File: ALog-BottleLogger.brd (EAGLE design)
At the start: 120.7 x 44.5 mm, 102 parts, among them IC2 ATMEGA644M, Q1 220mA/50V/3.5Ω, Q11 220mA/50V/3.5Ω, Q12 4.3A/20V/54mΩ, Q5 4.3A/20V/54mΩ, Q6 4.3A/20V/54mΩ, Q7 4.3A/20V/54mΩ, Q8 220mA/50V/3.5Ω, Q9 220mA/50V/3.5Ω, U2 FT231X-Q

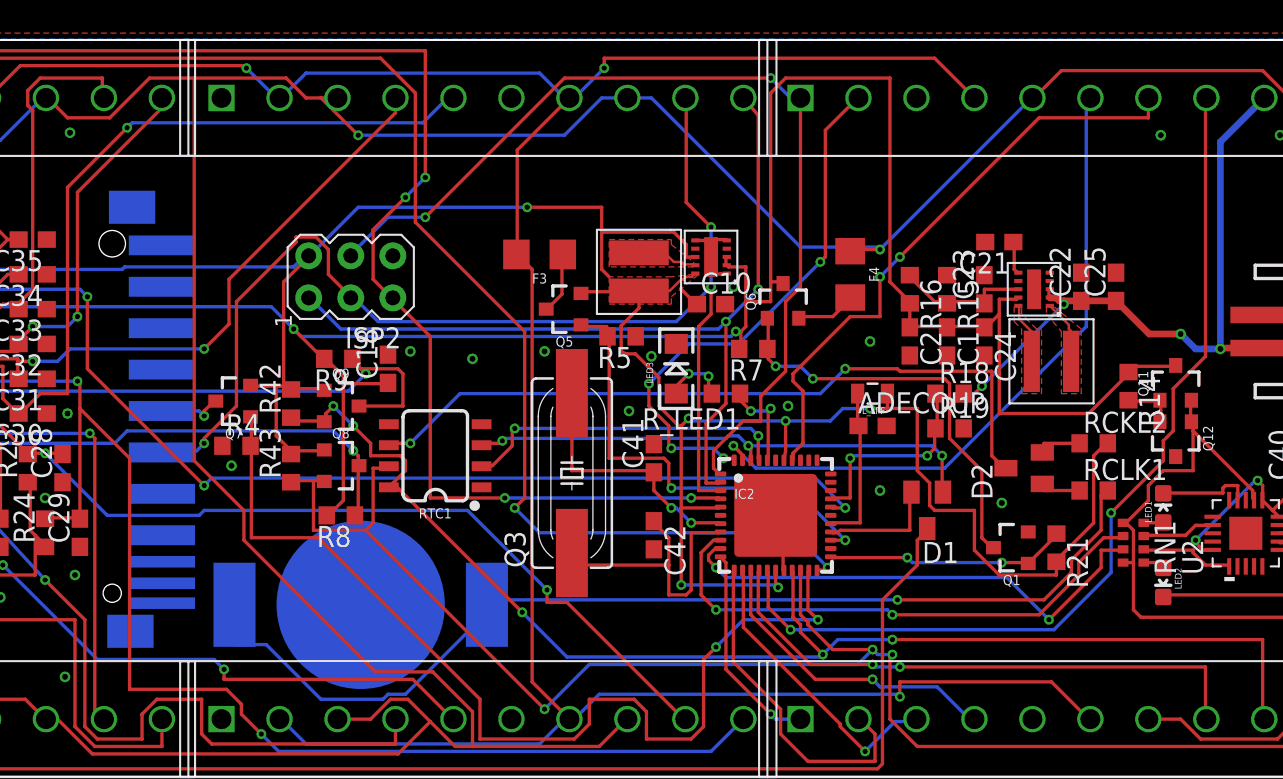
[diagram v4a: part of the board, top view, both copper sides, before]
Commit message: Changed cap sizes on 10 and 22 uF to 805 and fixed MISO/MOSI labels on SD card.
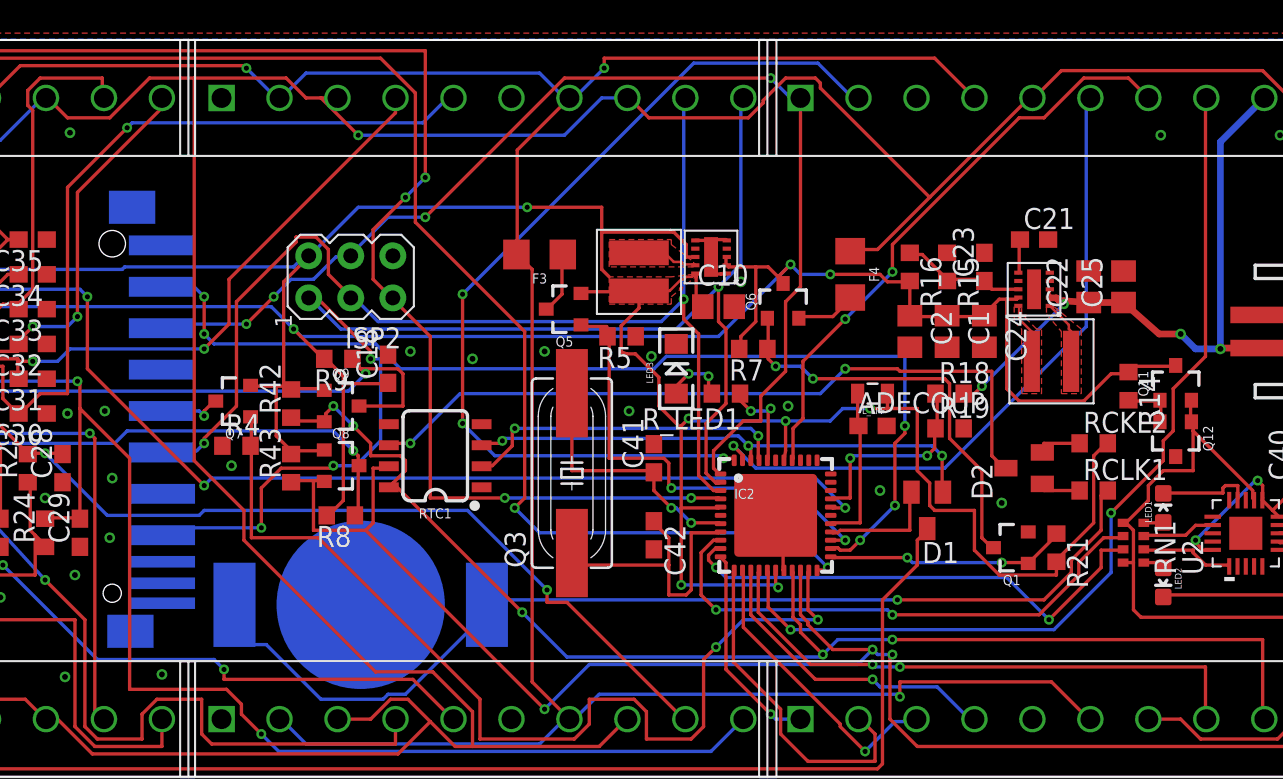
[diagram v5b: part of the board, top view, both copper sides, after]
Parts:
- C1, C10, C2, C22, C24, C25: device rcl:C0603 -> rcl:C0805
- C12, C13, C14, C15, C16, C17, C28, C29, C30, C31, C32, C33, C34, C35: value 10nF -> 0.1uF
- C23: value 10pF -> 33pF
- U$6: value TPS63061 -> TPS63060
- moved C21 2.11 mm to (93.8, 32.4), turned to 0 degrees
- moved C23 1.35 mm to (90.8, 30.8)
- moved R15 1.35 mm to (88.5, 30.8)
- moved R16 1.35 mm to (86.2, 30.8)
- moved C1 0.60 mm to (88.5, 26.9)
- moved C2 0.60 mm to (86.2, 26.9)
- moved C24 0.60 mm to (90.8, 26.9)
- moved C10 0.47 mm to (74.7, 28.4)
- moved C22 0.45 mm to (97.0, 29.6)
- moved C25 0.45 mm to (99.2, 29.6)
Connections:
- removed net D21: IC2.24
- removed net MISO/D5: SD.7
- removed net MOSI/D6: SD.2
- net MISO/D6: now also SD.7
- net MOSI/D5: now also SD.2
- net SD_CS: now also IC2.24
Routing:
- net SD_CS: track 0.00 -> 62.8 mm, vias 0 -> 5
- net MISO/D6: track 51.9 -> 79.8 mm, vias 2 -> 4
- net SS/D4: track 32.9 -> 55.7 mm, vias 4 -> 3
- net +5V: track 140.9 -> 119.8 mm, vias 3 -> 4
- net MOSI/D5: track 57.8 -> 71.1 mm, vias 2 -> 4
- net EXT_5V: track 279.6 -> 283.4 mm, vias 2 -> 1
- net SCK/D7: track 72.6 -> 69.6 mm, vias 3 -> 2
- net +3V3: track 172.1 -> 172.9 mm
- net MCU_ADC0: track 36.2 -> 35.6 mm
- net N$22: track 8.22 -> 7.71 mm
- net GND: vias 26 -> 29

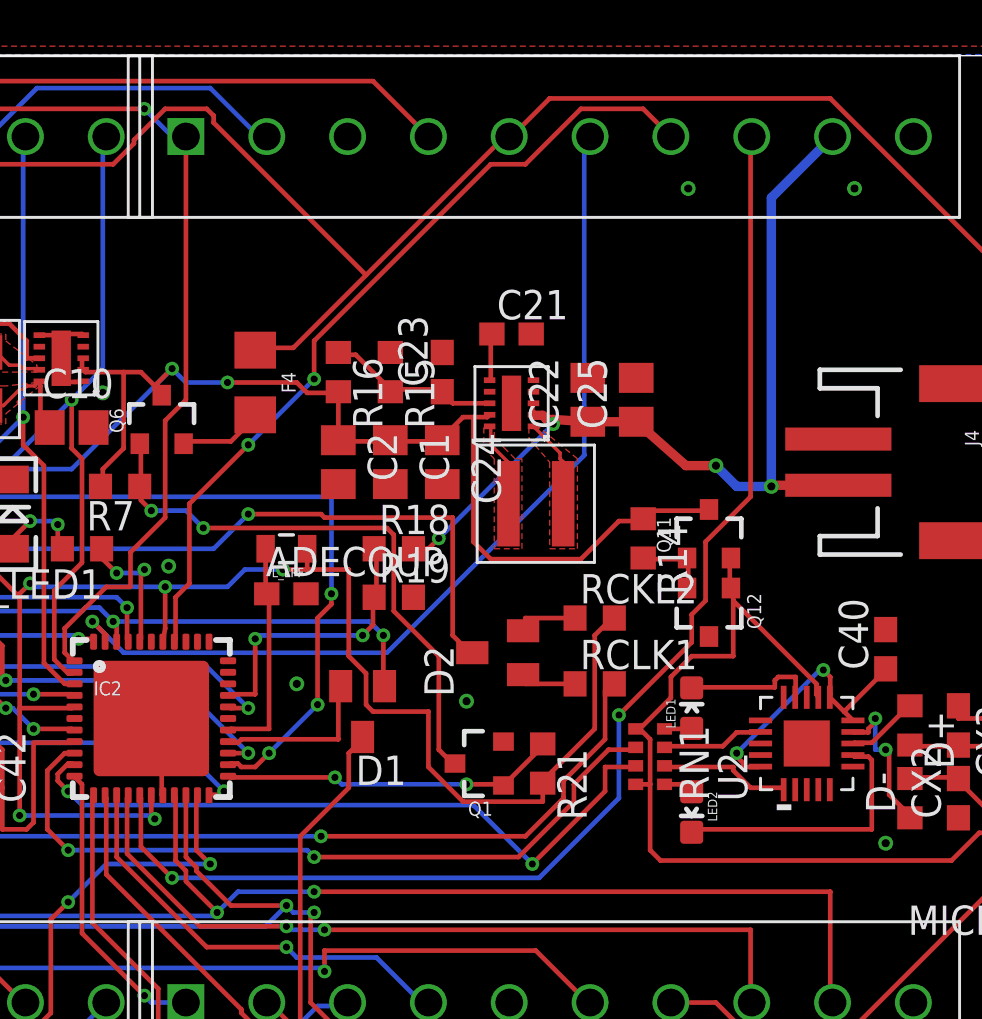
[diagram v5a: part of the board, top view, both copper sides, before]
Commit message: Corrected footprint of 5V regulator
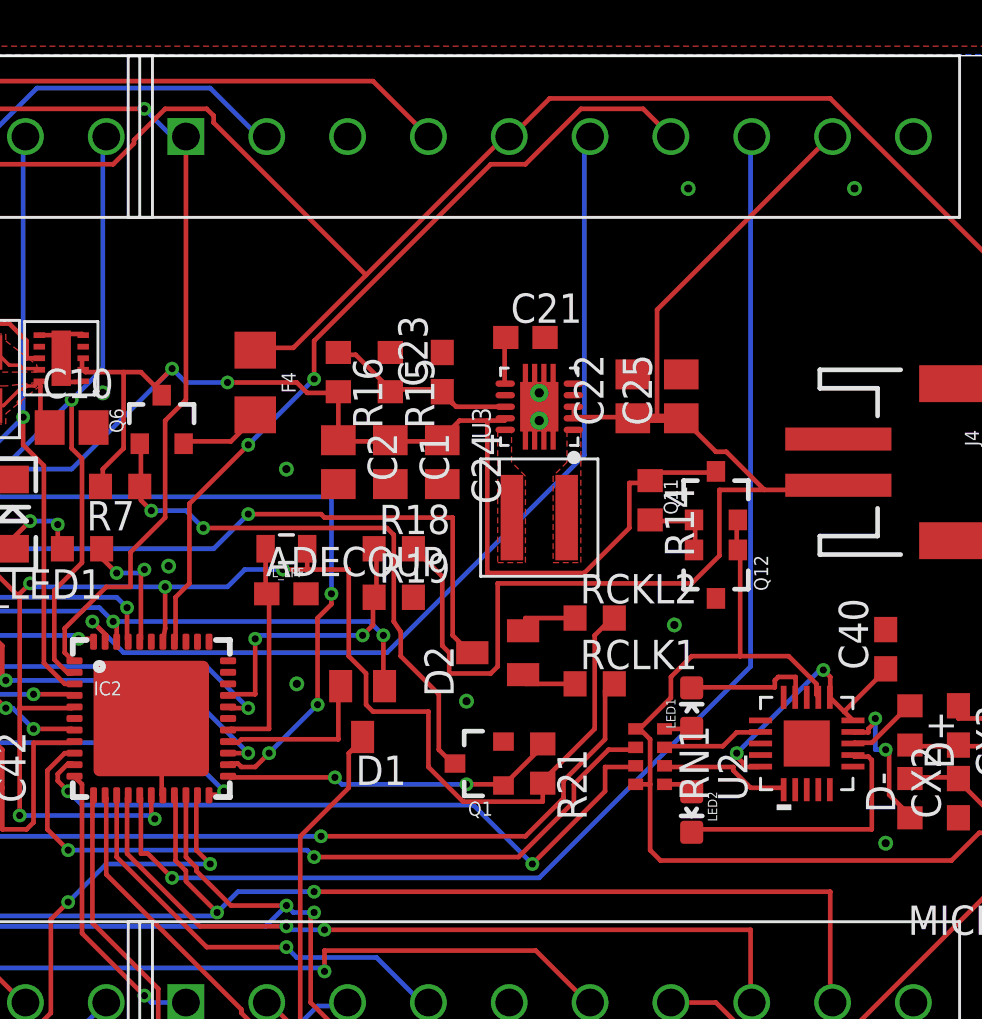
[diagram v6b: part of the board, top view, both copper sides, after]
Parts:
- removed U$6: TPS63060, Custom:WSON-10
- added U3: TPS63060, microbuilder:PWSON-N10
- moved C22 1.96 mm to (99.0, 29.7)
- moved C25 1.96 mm to (101.1, 29.7)
- moved Q11 1.68 mm to (102.6, 25.4)
- moved Q12 1.68 mm to (102.6, 22.1)
- moved R14 1.68 mm to (99.8, 25.2)
- moved U$9 0.62 mm to (95.0, 24.4)
- moved C21 0.62 mm to (94.3, 32.2)
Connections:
- removed net N$19: U$6.P$10, U$9.P$2
- removed net N$20: U$6.P$1, U$9.P$1
- new net N$27: U$9.P$1, U3.1
- new net N$32: U$9.P$2, U3.10
- net +5V: now also U3.9; no longer U$6.P$9
- net BATT+: now also U3.2, U3.3; no longer U$6.P$2, U$6.P$3
- net GND: now also U3.7, U3.THERMAL@1, U3.THERMAL@10, U3.THERMAL@11, U3.THERMAL@12, U3.THERMAL@13, U3.THERMAL@14, U3.THERMAL@5, U3.THERMAL@6, U3.THERMAL@7, U3.THERMAL@8, U3.THERMAL@9; no longer U$6.P$11, U$6.P$4, U$6.P$7
- net N$21: now also U3.6; no longer U$6.P$6
- net N$22: now also U3.8; no longer U$6.P$8
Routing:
- net BATT+: track 39.7 -> 55.5 mm, vias 4 -> 0
- net N$20: track 3.88 -> 0.00 mm
- net N$19: track 3.69 -> 0.00 mm
- net +5V: track 119.8 -> 123.1 mm
- net N$22: track 7.71 -> 9.12 mm
- net VUSB: track 39.2 -> 39.8 mm
- net D15~: track 56.0 -> 56.2 mm, vias 2 -> 1
- net GND: vias 29 -> 31
- added copper zone on layer 1, net N$27
- added copper zone on layer 1, net N$32
- removed copper zone on layer 1, net N$19
- removed copper zone on layer 1, net N$20

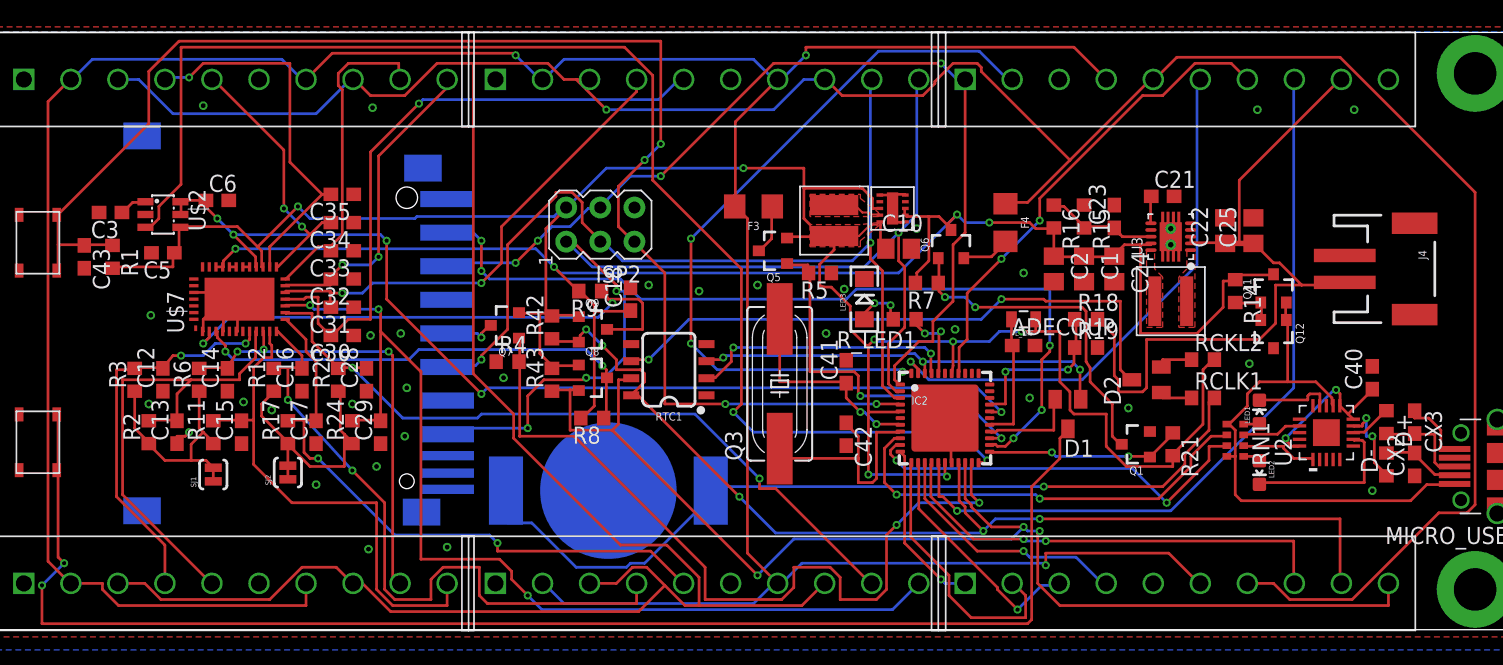
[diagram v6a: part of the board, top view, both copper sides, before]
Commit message: Changed 3.3 voltage regulator to TPS62172
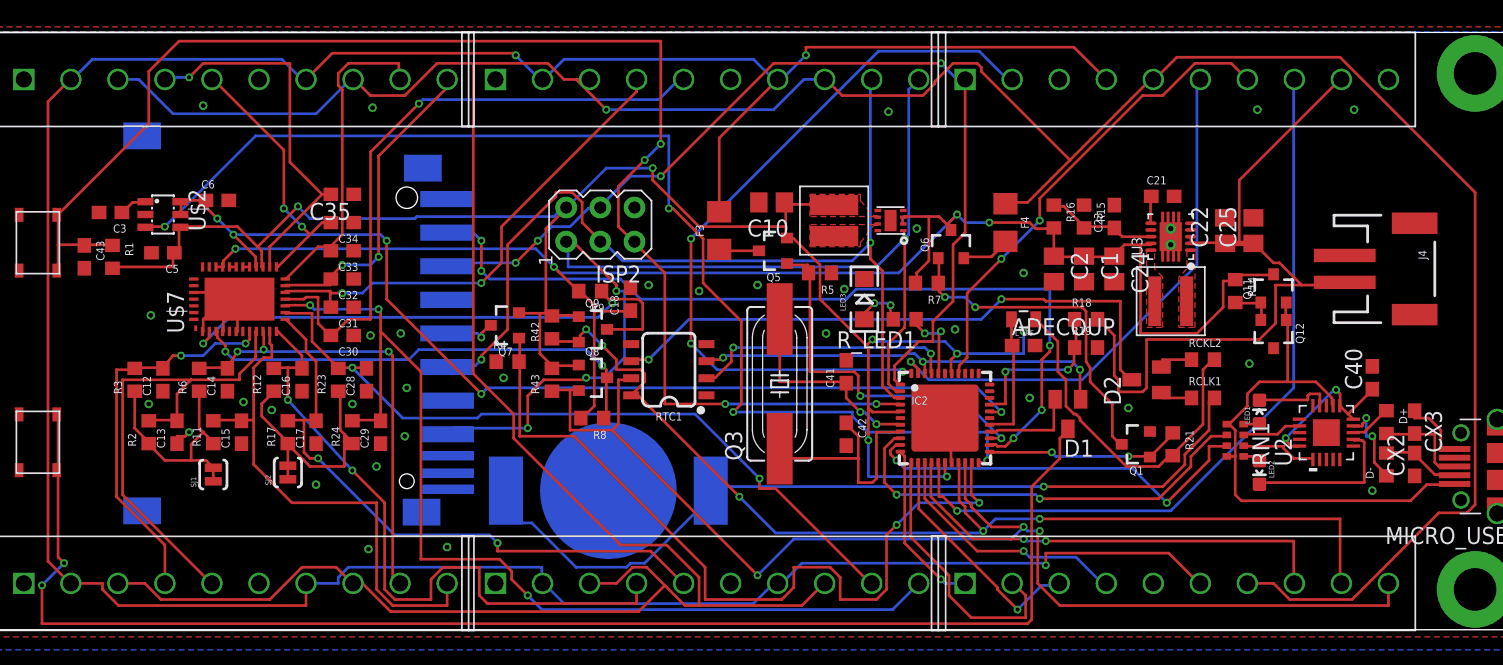
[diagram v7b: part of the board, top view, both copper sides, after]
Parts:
- R1, R11, R12, R14, R15, R16, R17, R18, R19, R2, R21, R23, R24, R3, R4, R42, R43, R5, R6, R7, R8, R9: device rcl:R0603@1 -> rcl:R0603
- U$3: value TPS6217X -> TPS62172; device texas:WSON-10 -> SparkFun-IC-Power:WSON-8-PAD
- moved C10 10.1 mm to (65.2, 31.8), turned to 180 degrees
- moved F3 3.12 mm to (61.4, 29.7), turned to 90 degrees
- moved U$3 0.91 mm to (74.1, 30.4), turned to 90 degrees
- turned L1 to 90 degrees
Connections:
- net +3V3: now also U$3.6; no longer U$3.P$10, U$3.P$8
- net +5V: now also U$3.2, U$3.3; no longer U$3.P$2, U$3.P$3
- net GND: now also U$3.1, U$3.4, U$3.5, U$3.PAD; no longer U$3.P$1, U$3.P$11, U$3.P$4, U$3.P$5, U$3.P$6
- net N$1: now also U$3.7; no longer U$3.P$9
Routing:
- net 1.8V_EN: track 99.9 -> 87.5 mm, vias 2 -> 4
- net +3V3: track 172.9 -> 161.2 mm
- net EXT_3.3V: track 235.5 -> 226.6 mm
- net GND: track 28.8 -> 23.8 mm, vias 31 -> 32
- net N$1: track 3.71 -> 0.36 mm
- net MISO/D6: track 79.8 -> 80.6 mm
- net N$17: track 3.77 -> 3.05 mm

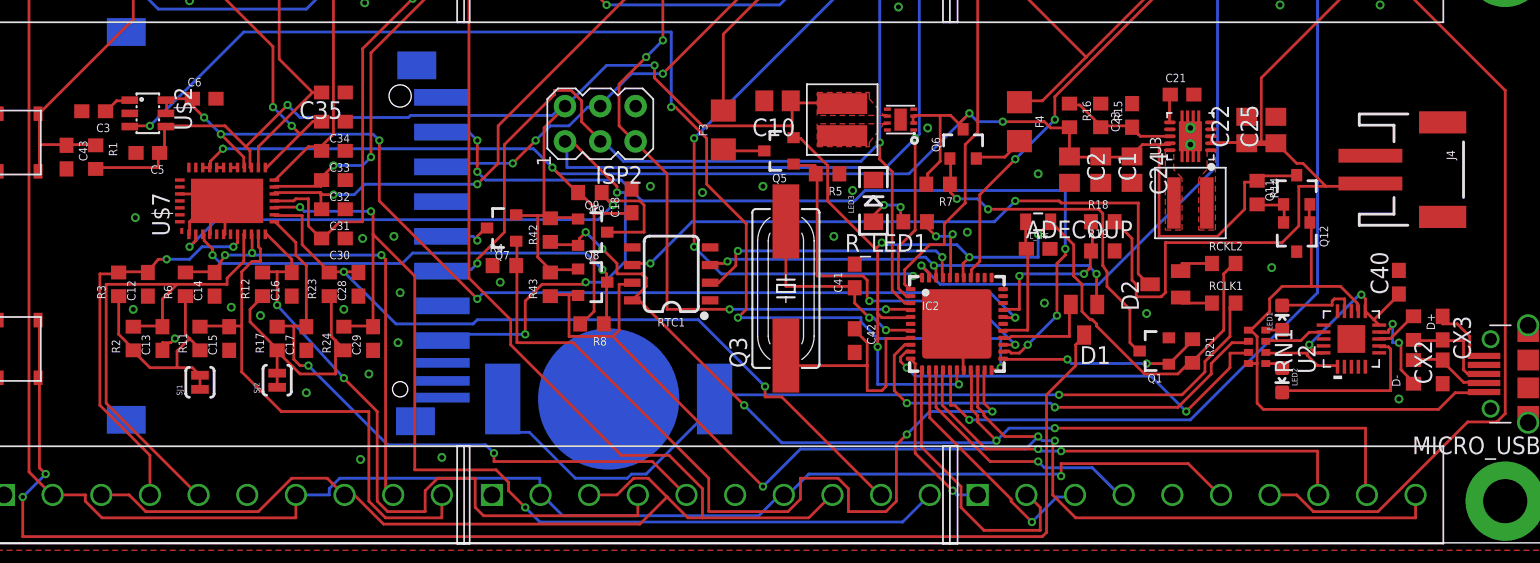
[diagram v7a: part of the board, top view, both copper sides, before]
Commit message: Fixed USB FTDI mosphet connections, updated 3.3V regulator, fixed ground connection on 1.8V reg
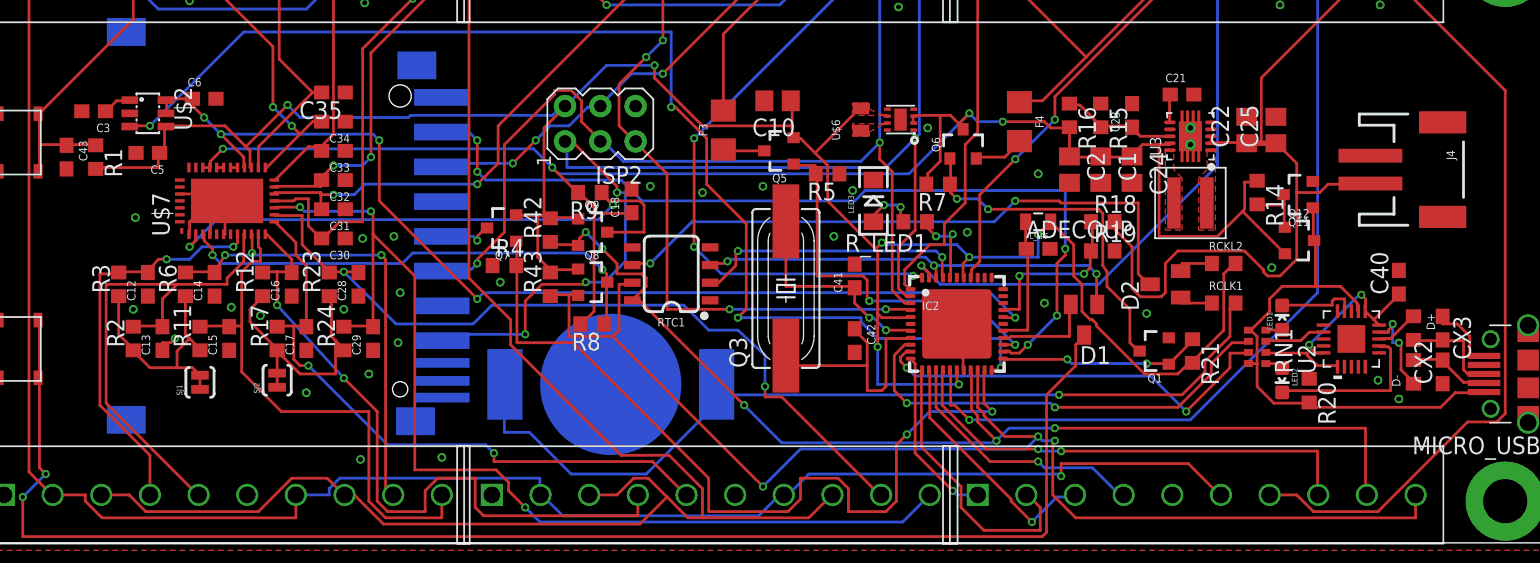
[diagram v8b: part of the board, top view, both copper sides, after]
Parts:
- removed L1: 10uH, Custom:WE-LQS(INDUCTOR)
- added R20: 10k, rcl:R0603@1
- added U$6: 74404020022, csandell:WURTH2.2UF
- R1, R11, R12, R14, R15, R16, R17, R18, R19, R2, R21, R23, R24, R3, R4, R42, R43, R5, R6, R7, R8, R9: device rcl:R0603 -> rcl:R0603@1
- moved CLOCK_BATT 1.06 mm to (53.2, 11.4)
- moved Q11 0.34 mm to (102.8, 25.1), turned to 90 degrees
- moved Q12 0.34 mm to (102.8, 21.8), turned to 270 degrees
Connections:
- removed net N$9: U$2.2
- net +3V3: now also U$6.2; no longer L1.P$2
- net +5V: now also Q12.2; no longer Q11.3
- net GND: now also Q11.2, R20.1, U$2.2; no longer Q12.3
- net N$1: now also U$6.1; no longer L1.P$1
- net N$11: now also Q11.3, Q12.1; no longer Q11.1, Q12.2
- net VUSB: now also Q11.1, Q12.3, R20.2; no longer Q11.2, Q12.1
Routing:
- net ADC6: track 55.1 -> 57.2 mm
- net RTC_BATT: track 65.1 -> 67.0 mm
- net +5V: track 123.2 -> 124.6 mm
- net N$11: track 3.30 -> 4.41 mm
- net BATT+: track 55.5 -> 56.5 mm
- net VUSB: track 39.8 -> 38.9 mm
- net GND: vias 32 -> 33
